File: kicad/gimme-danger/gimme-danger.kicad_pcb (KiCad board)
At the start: 4 copper layers, 46.1 x 30 mm, 69 parts, among them J3 Screw_Terminal_01x06, Q1 AO3400A, Q2 AO3400A, Q3 AO3400A, Q4 AO3400A, U1 ESP32-S3-WROOM-1, U2 TPD6S300RUKR, U3 U261-241N-4BS2SS, U4 AO4407A, U5 SKRKAEE020, U6 DDTC143EUA, U7 SKRKAEE020, U8 TPS54302

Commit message: v0.0.1a maybe?
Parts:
- added kibuzzard-65EADF23: G***, kibuzzard-65EADF23, F.Cu at (87.5, 114.0)
- added kibuzzard-65EADF47: G***, kibuzzard-65EADF47, F.Cu at (87.3, 121.5)
- added kibuzzard-65EB0655: G***, kibuzzard-65EB0655, B.Cu at (78.6, 99.4)
- added kibuzzard-65EB08A1: G***, kibuzzard-65EB08A1, F.Cu at (78.4, 115.5)
- added kibuzzard-65EB08B9: G***, kibuzzard-65EB08B9, F.Cu at (82.8, 115.5)
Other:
- outline, holes or cut-outs redrawn
- board text added: "GIMME DANGER!!"

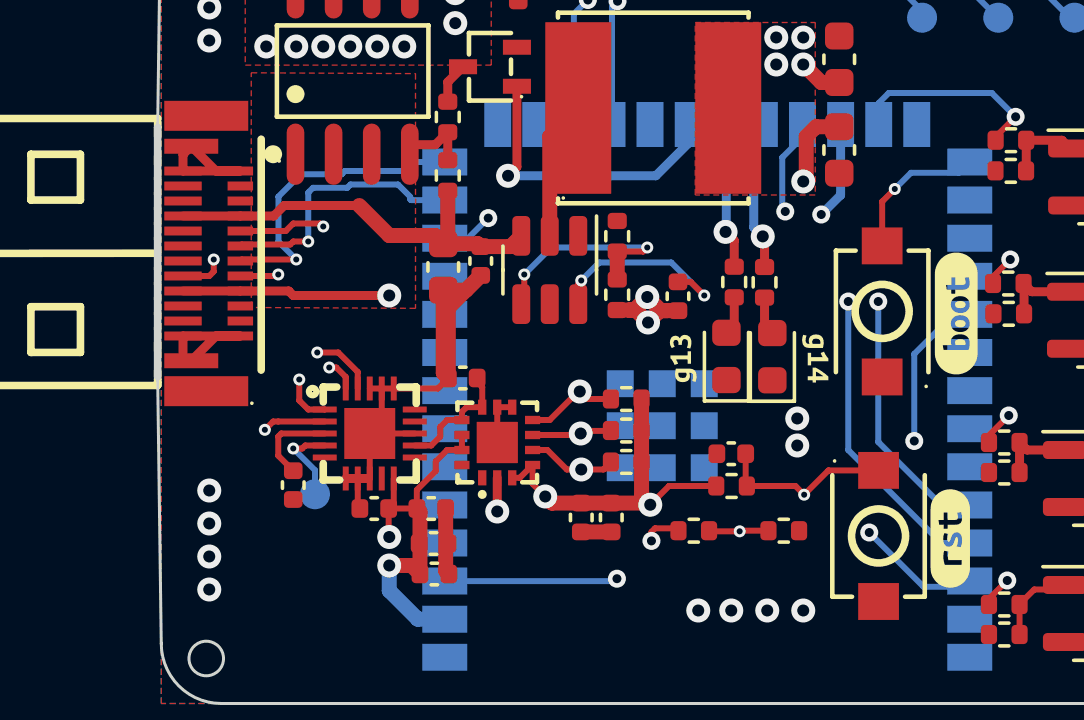
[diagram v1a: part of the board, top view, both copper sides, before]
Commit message: No mo 0.2 vias -> 0.3 vias
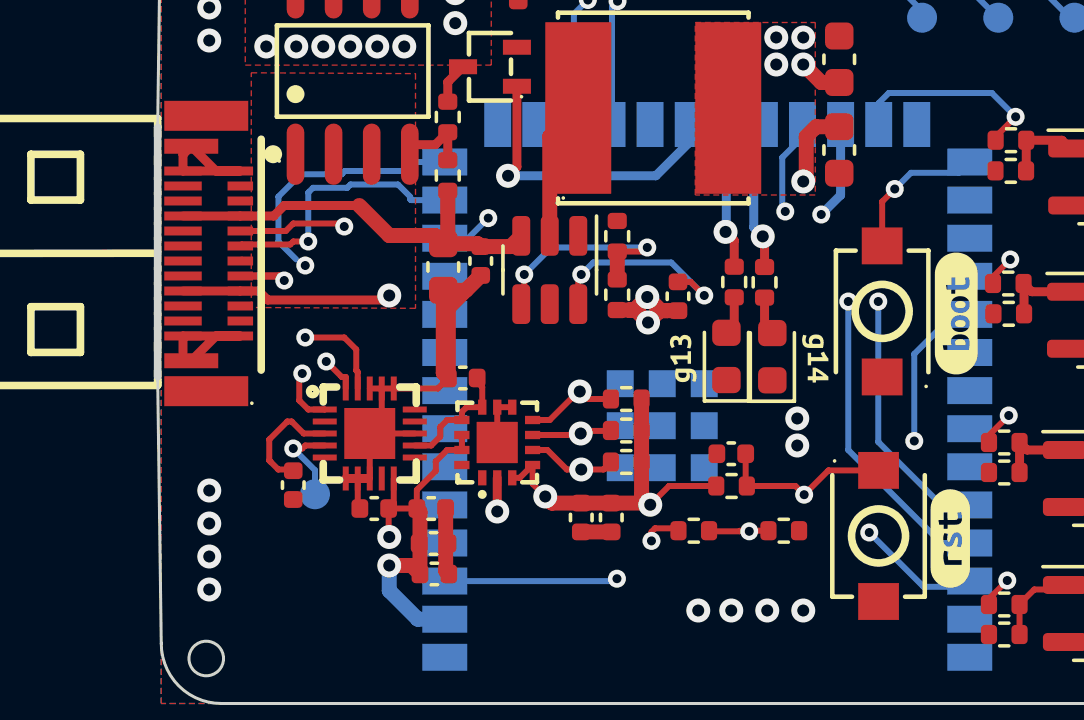
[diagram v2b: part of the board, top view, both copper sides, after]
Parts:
- C1: value 100n -> 0.1u
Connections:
- U2 pad 2: C_SBU2 -> unconnected-(U2-C_SBU2-Pad2)
- U3 pad B8: C_SBU2 -> unconnected-(U3-SBU2-PadB8)
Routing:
- net C_SBU2: track 10.4 -> 0.00 mm, vias 2 -> 0
- net D+: track 15.9 -> 14.6 mm
- net Net-(U2-VBIAS): track 2.94 -> 3.91 mm
- net C_SBU1: track 11.7 -> 12.5 mm
- net VMON: track 10.5 -> 9.90 mm
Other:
- board text added: "JLCJLCJLCJLC"

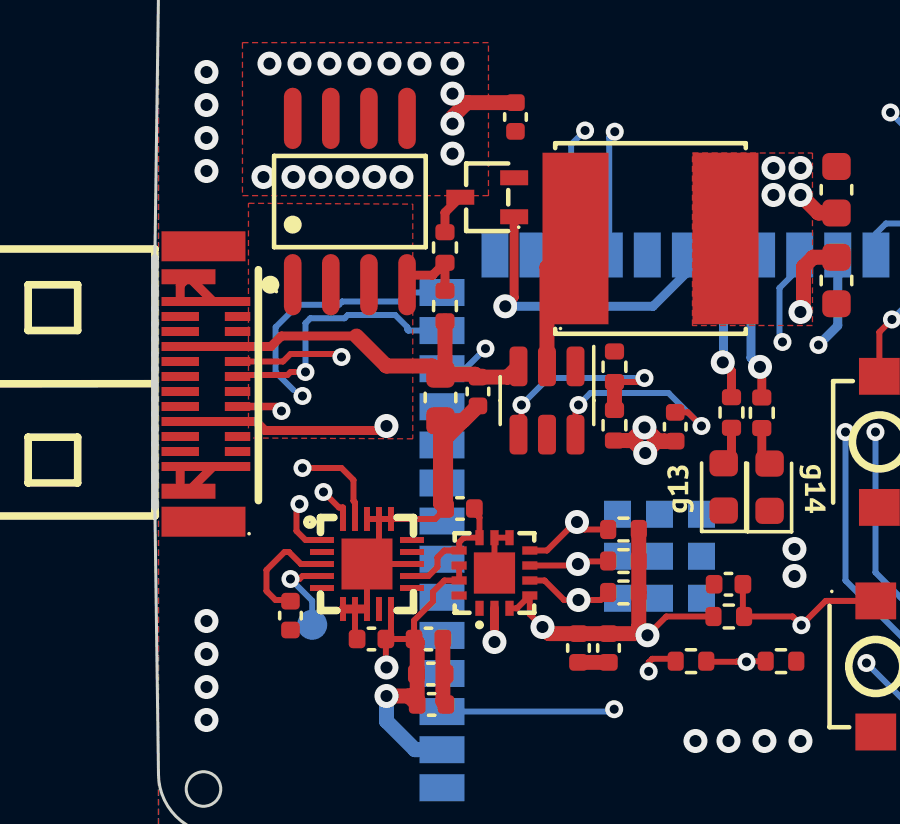
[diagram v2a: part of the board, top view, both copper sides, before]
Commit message: Fixes DRC errors
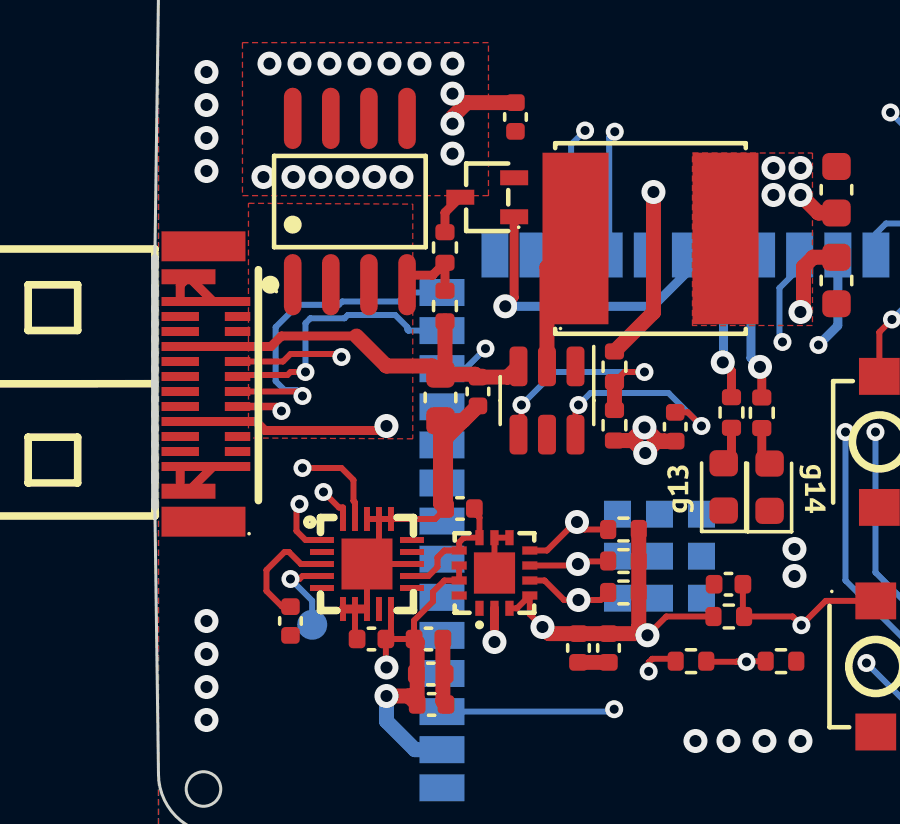
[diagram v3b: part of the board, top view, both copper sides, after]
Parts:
- moved C1 0.18 mm to (65.4, 119.9)
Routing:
- net GND: track 31.7 -> 37.6 mm, vias 14 -> 15
- net D+: track 14.6 -> 17.3 mm
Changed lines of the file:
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@@
     )
     (pad_to_mask_clearance 0)
+    (grid_origin 76.2 110.9)
     (pcbplotparams
       (layerselection 0x00010fc_ffffffff)
@@
   )
   (footprint "Capacitor_SMD:C_0402_1005Metric" (layer "F.Cu")
-    (at 65.4 119.72 -90)
+    (at 65.4 119.9 -90)
     (descr "Capacitor SMD 0402 (1005 Metric), square (rectangular) end terminal, IPC_7351 nominal, (Body size source: IPC-SM-782 page 76, https://www.pcb-3d.com/wordpress/wp-content/uploads/ipc-sm-782a_amendment_1_and_2.pdf), generated with kicad-footprint-generator")
     (tags "capacitor")
@@
   (segment (start 89.479557 107.444104) (end 88.685453 106.65) (width 0.2) (layer "B.Cu") (net 14))
   (segment (start 85.25 106.65) (end 84.915 106.985) (width 0.2) (layer "B.Cu") (net 14))
-  (segment (start 64.6 118.2) (end 64.6 118.9) (width 0.2) (layer "F.Cu") (net 41))
   (segment (start 66.45033 118.000127) (end 65.748656 118.000127) (width 0.2) (layer "F.Cu") (net 41))
-  (segment (start 65.748656 118.000127) (end 65.348529 117.6) (width 0.2) (layer "F.Cu") (net 41))
-  (segment (start 65.2 117.6) (end 64.6 118.2) (width 0.2) (layer "F.Cu") (net 41))
-  (segment (start 65.36 119.2) (end 65.4 119.24) (width 0.2) (layer "F.Cu") (net 41))
-  (segment (start 64.65 118.95) (end 64.9 119.2) (width 0.2) (layer "F.Cu") (net 41))
-  (segment (start 64.9 119.2) (end 65.36 119.2) (width 0.2) (layer "F.Cu") (net 41))
+  (segment (start 64.6 118.9) (end 65.12 119.42) (width 0.2) (layer "F.Cu") (net 41))
+  (segment (start 65.12 119.42) (end 65.4 119.42) (width 0.2) (layer "F.Cu") (net 41))
   (segment (start 65.348529 117.6) (end 65.2 117.6) (width 0.2) (layer "F.Cu") (net 41))
-  (segment (start 64.6 118.9) (end 64.65 118.95) (width 0.2) (layer "F.Cu") (net 41))
+  (segment (start 65.2 117.6) (end 64.6 118.2) (width 0.2) (layer "F.Cu") (net 41))
+  (segment (start 64.6 118.2) (end 64.6 118.9) (width 0.2) (layer "F.Cu") (net 41))
+  (segment (start 65.748656 118.000127) (end 65.348529 117.6) (width 0.2) (layer "F.Cu") (net 41))
   (segment (start 70.48 122.578) (end 70.584 122.682) (width 0.5) (layer "F.Cu") (net 42))
   (segment (start 72.2 117.122454) (end 72.700127 117.122454) (width 0.2) (layer "F.Cu") (net 42))
@@
   (segment (start 70.4 115.98) (end 70.57 116.15) (width 0.5) (layer "F.Cu") (net 42))
   (segment (start 61.724917 114.749936) (end 61.724917 115.299847) (width 0.3) (layer "F.Cu") (net 42))
+  (segment (start 77.5 109.615) (end 77.5 105.6) (width 0.5) (layer "F.Cu") (net 42))
   (segment (start 67.550152 119.5) (end 67.550152 120.430152) (width 0.2) (layer "F.Cu") (net 42))
   (segment (start 70.4 113.225) (end 70.4 115.98) (width 0.5) (layer "F.Cu") (net 42))
+  (segment (start 76.2 110.915) (end 77.5 109.615) (width 0.5) (layer "F.Cu") (net 42))
   (segment (start 76 121.28) (end 75 121.28) (width 0.5) (layer "F.Cu") (net 42))
   (segment (start 71.65 112.73) (end 70.57 113.81) (width 0.5) (layer "F.Cu") (net 42))
@@
   (segment (start 68.350254 117.600076) (end 67.950203 118.000127) (width 0.2) (layer "F.Cu") (net 42))
   (via (at 62.6 103.8) (size 0.8) (drill 0.4) (layers "F.Cu" "B.Cu") (free) (net 42))
+  (via (at 77.5 105.6) (size 0.8) (drill 0.4) (layers "F.Cu" "B.Cu") (net 42))
   (via (at 62.6 102.7) (size 0.8) (drill 0.4) (layers "F.Cu" "B.Cu") (free) (net 42))
   (via (at 62.6 123.2) (size 0.8) (drill 0.4) (layers "F.Cu" "B.Cu") (free) (net 42))
@@
   (segment (start 87.95 108.95) (end 87.59 109.31) (width 0.2) (layer "B.Cu") (net 61))
   (segment (start 67.5 115.9) (end 67.550406 115.950406) (width 0.2) (layer "F.Cu") (net 62))
+  (segment (start 65.8 112.4) (end 65.650064 112.250064) (width 0.2) (layer "F.Cu") (net 62))
   (segment (start 65.8 114.8) (end 67.1 114.8) (width 0.2) (layer "F.Cu") (net 62))
   (segment (start 63.635001 112.250064) (end 63.685065 112.2) (width 0.2) (layer "F.Cu") (net 62))
@@
   (segment (start 67.1 114.8) (end 67.5 115.2) (width 0.2) (layer "F.Cu") (net 62))
   (segment (start 65.8 112.2) (end 66 112.4) (width 0.2) (layer "F.Cu") (net 62))
+  (segment (start 65.650064 112.250064) (end 63.635001 112.250064) (width 0.2) (layer "F.Cu") (net 62))
   (via (at 65.8 114.8) (size 0.6) (drill 0.3) (layers "F.Cu" "B.Cu") (net 62))
   (via (at 65.8 112.4) (size 0.6) (drill 0.3) (layers "F.Cu" "B.Cu") (net 62))
@@
   (segment (start 66.1 114.5) (end 65.8 114.8) (width 0.2) (layer "In2.Cu") (net 62))
   (segment (start 66.1 112.7) (end 65.8 112.4) (width 0.2) (layer "In2.Cu") (net 62))
+  (segment (start 65.2 112.2) (end 64.905 111.905) (width 0.2) (layer "B.Cu") (net 62))
+  (segment (start 65.8 112.4) (end 65.6 112.2) (width 0.2) (layer "B.Cu") (net 62))
+  (segment (start 69.02498 109.250019) (end 69.324999 108.95) (width 0.2) (layer "B.Cu") (net 62))
+  (segment (start 65.65 109.36) (end 67.01368 109.36) (width 0.2) (layer "B.Cu") (net 62))
+  (segment (start 65.6 112.2) (end 65.2 112.2) (width 0.2) (layer "B.Cu") (net 62))
   (segment (start 67.123661 109.250019) (end 69.02498 109.250019) (width 0.2) (layer "B.Cu") (net 62))
   (segment (start 67.01368 109.36) (end 67.123661 109.250019) (width 0.2) (layer "B.Cu") (net 62))
-  (segment (start 64.905 110.105) (end 65.65 109.36) (width 0.2) (layer "B.Cu") (net 62))
-  (segment (start 65.65 109.36) (end 67.01368 109.36) (width 0.2) (layer "B.Cu") (net 62))
   (segment (start 69.324999 108.95) (end 70.45 108.95) (width 0.2) (layer "B.Cu") (net 62))
-  (segment (start 65.5 112.2) (end 64.905 111.605) (width 0.2) (layer "B.Cu") (net 62))
-  (segment (start 69.02498 109.250019) (end 69.324999 108.95) (width 0.2) (layer "B.Cu") (net 62))
-  (segment (start 64.905 111.605) (end 64.905 110.105) (width 0.2) (layer "B.Cu") (net 62))
+  (segment (start 64.905 111.905) (end 64.905 110.105) (width 0.2) (layer "B.Cu") (net 62))
+  (segment (start 64.905 110.105) (end 65.65 109.36) (width 0.2) (layer "B.Cu") (net 62))
   (segment (start 67.150355 116.116041) (end 67.150355 116.5) (width 0.2) (layer "F.Cu") (net 63))
   (segment (start 67.016041 116.116041) (end 66.5 115.6) (width 0.2) (layer "F.Cu") (net 63))
@@
   (segment (start 73.95 111.4125) (end 73.95 108.1) (width 0.5) (layer "F.Cu") (net 69))
   (segment (start 73.95 108.1) (end 74.9 107.15) (width 0.5) (layer "F.Cu") (net 69))
+  (segment (start 76.535 111.6) (end 76.2 111.935) (width 0.2) (layer "F.Cu") (net 70))
+  (segment (start 77.2 111.6) (end 76.535 111.6) (width 0.2) (layer "F.Cu") (net 70))
   (segment (start 73.1 112.7) (end 73.1 113.5875) (width 0.2) (layer "F.Cu") (net 70))
-  (segment (start 77.065 111.935) (end 77.2 111.8) (width 0.2) (layer "F.Cu") (net 70))
   (segment (start 76.2 111.935) (end 76.2 112.865) (width 0.5) (layer "F.Cu") (net 70))
   (segment (start 73.1 113.5875) (end 73 113.6875) (width 0.2) (layer "F.Cu") (net 70))
-  (segment (start 76.2 111.935) (end 77.065 111.935) (width 0.2) (layer "F.Cu") (net 70))
   (via (at 73.1 112.7) (size 0.6) (drill 0.3) (layers "F.Cu" "B.Cu") (net 70))
-  (via (at 77.2 111.8) (size 0.6) (drill 0.3) (layers "F.Cu" "B.Cu") (net 70))
-  (segment (start 77.2 111.8) (end 74 111.8) (width 0.2) (layer "B.Cu") (net 70))
-  (segment (start 74 111.8) (end 73.1 112.7) (width 0.2) (layer "B.Cu") (net 70))
+  (via (at 77.2 111.6) (size 0.6) (drill 0.3) (layers "F.Cu" "B.Cu") (net 70))
+  (segment (start 77.2 111.6) (end 74.2 111.6) (width 0.2) (layer "B.Cu") (net 70))
+  (segment (start 74.2 111.6) (end 73.1 112.7) (width 0.2) (layer "B.Cu") (net 70))
   (segment (start 72.9 102.62) (end 71.28 102.62) (width 0.5) (layer "F.Cu") (net 72))
   (segment (start 77.46 121.16) (end 78.16 121.16) (width 0.2) (layer "F.Cu") (net 72))
